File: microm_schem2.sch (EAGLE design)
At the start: 81 parts, among them Q1 16 MHz

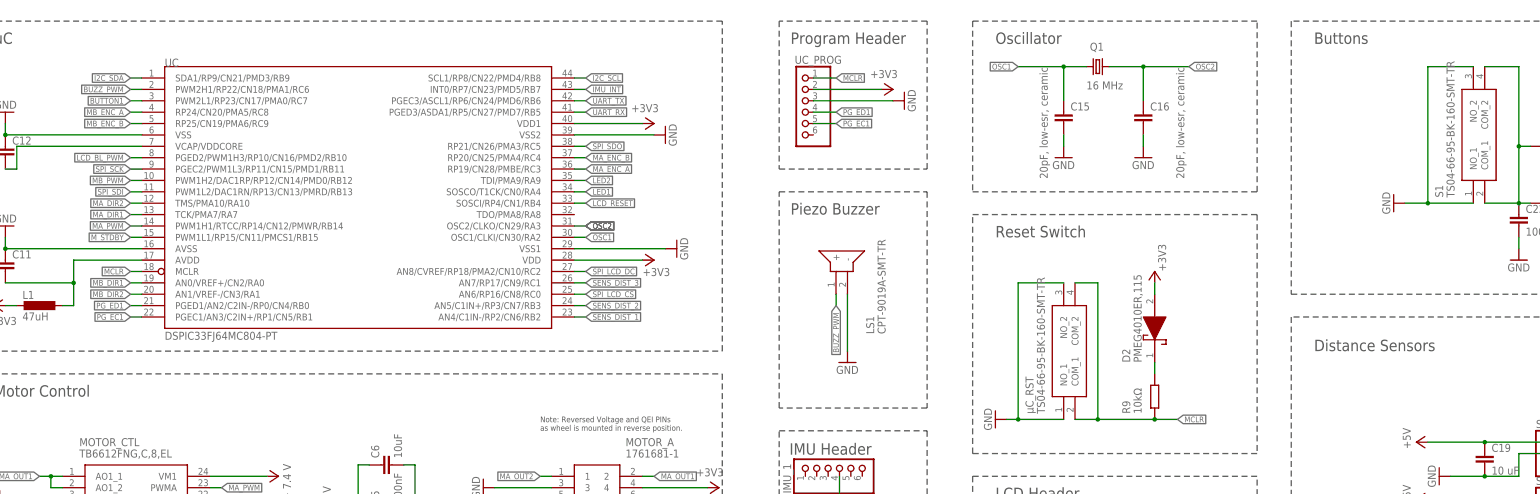
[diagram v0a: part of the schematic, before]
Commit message: Improve 3.3V routing.
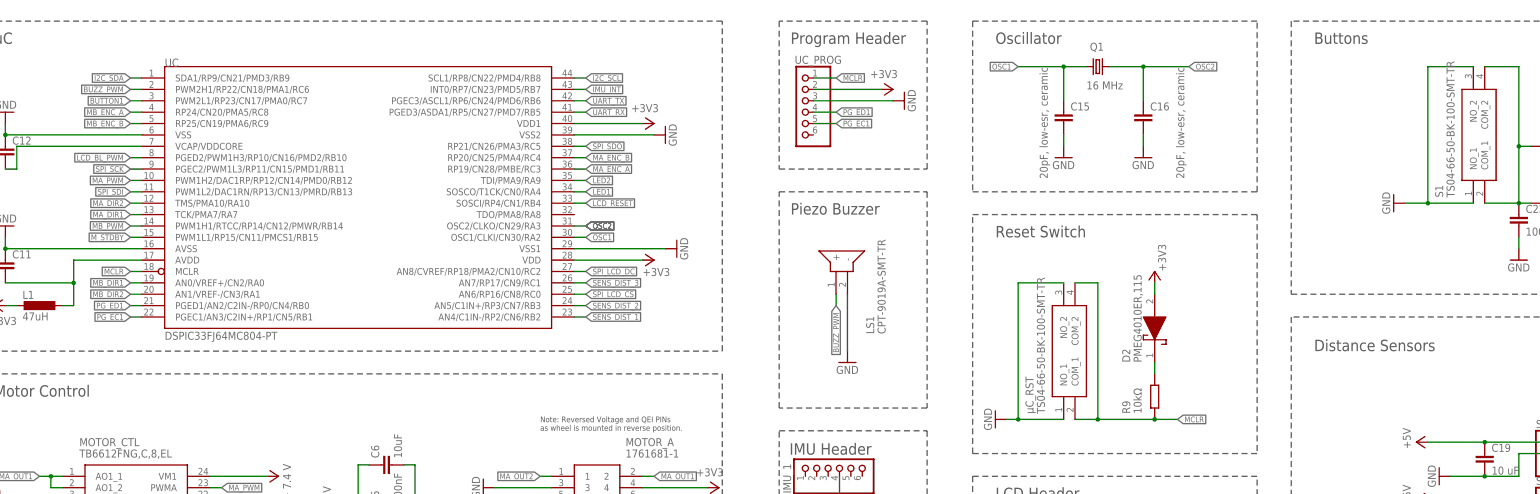
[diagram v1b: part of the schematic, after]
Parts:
- S1, µC_RST: value TS04-66-95-BK-160-SMT-TR -> TS04-66-50-BK-100-SMT-TR; device SamacSys_Parts:TS04-66-95-BK-160-SMT-TR -> SamacSys_Parts:TS04-66-50-BK-100-SMT-TR
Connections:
- net MA_PWM: now also UC.PWM1H2/DAC1RP/RP12/CN14/PMD0/RB12; no longer UC.PWM1H1/RTCC/RP14/CN12/PMWR/RB14
- net MB_PWM: now also UC.PWM1H1/RTCC/RP14/CN12/PMWR/RB14; no longer UC.PWM1H2/DAC1RP/RP12/CN14/PMD0/RB12

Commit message: Add most recent board version
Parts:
- removed H1, H2: MOUNT-PAD-ROUND2.8, holes:MOUNT-PAD-ROUND2.8
- removed LCD: (no value), pinhead:PINHD-1X11
- removed SPI: (no value), pinhead:PINHD-2X4
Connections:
- removed net LCD_BL_PWM: LCD.11, UC.PGED2/PWM1H3/RP10/CN16/PMD2/RB10
- removed net LCD_RESET: LCD.8, UC.SOSCI/RP4/CN1/RB4
- removed net SPI_LCD_CS: LCD.7, SPI.2, UC.AN6/RP16/CN8/RC0
- removed net SPI_LCD_DC: LCD.9, UC.AN8/CVREF/RP18/PMA2/CN10/RC2
- removed net SPI_SCK: LCD.4, SPI.1, UC.PGEC2/PWM1L3/RP11/CN15/PMD1/RB11
- removed net SPI_SDI: LCD.6, SPI.5, UC.PWM1L2/DAC1RN/RP13/CN13/PMRD/RB13
- removed net SPI_SDO: LCD.5, SPI.3, UC.RP21/CN26/PMA3/RC5
- removed net SPI_SD_CS: LCD.10, SPI.4
- net +3V3: now also BT_CON.A; no longer BT_CON.C, LCD.1, SPI.7
- net GND: no longer H1.MOUNT, H2.MOUNT, LCD.3, SPI.8
- net MA_ENC_A: now also UC.RP24/CN20/PMA5/RC8; no longer UC.RP19/CN28/PMBE/RC3
- net MA_ENC_B: now also UC.RP25/CN19/PMA6/RC9; no longer UC.RP20/CN25/PMA4/RC4
- net MB_ENC_A: now also UC.AN5/C1IN+/RP3/CN7/RB3; no longer UC.RP24/CN20/PMA5/RC8
- net MB_ENC_B: now also UC.AN4/C1IN-/RP2/CN6/RB2; no longer UC.RP25/CN19/PMA6/RC9
- net N$1: now also BT_CON.C; no longer BT_CON.A
- net SENS_DIST_1: now also UC.AN6/RP16/CN8/RC0; no longer UC.AN4/C1IN-/RP2/CN6/RB2
- net SENS_DIST_2: now also UC.AN7/RP17/CN9/RC1; no longer UC.AN5/C1IN+/RP3/CN7/RB3
- net SENS_DIST_3: now also UC.AN8/CVREF/RP18/PMA2/CN10/RC2; no longer UC.AN7/RP17/CN9/RC1
- net UART_TX: now also UC.SOSCI/RP4/CN1/RB4; no longer UC.PGEC3/ASCL1/RP6/CN24/PMD6/RB6
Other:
- note removed: "LCD Header"
- moved on the sheet: BT_CON
